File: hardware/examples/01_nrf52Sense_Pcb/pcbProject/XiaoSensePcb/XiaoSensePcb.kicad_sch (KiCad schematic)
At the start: 1 part, among them U1 Seeed Studio XIAO nRF52840

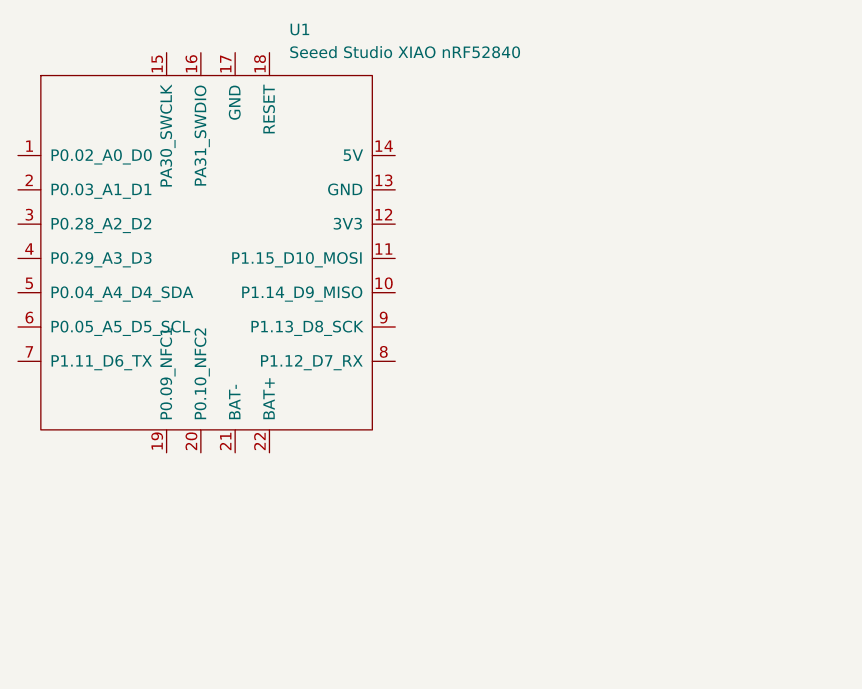
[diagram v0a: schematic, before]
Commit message: Adding kicad files for xiao sense pcb board
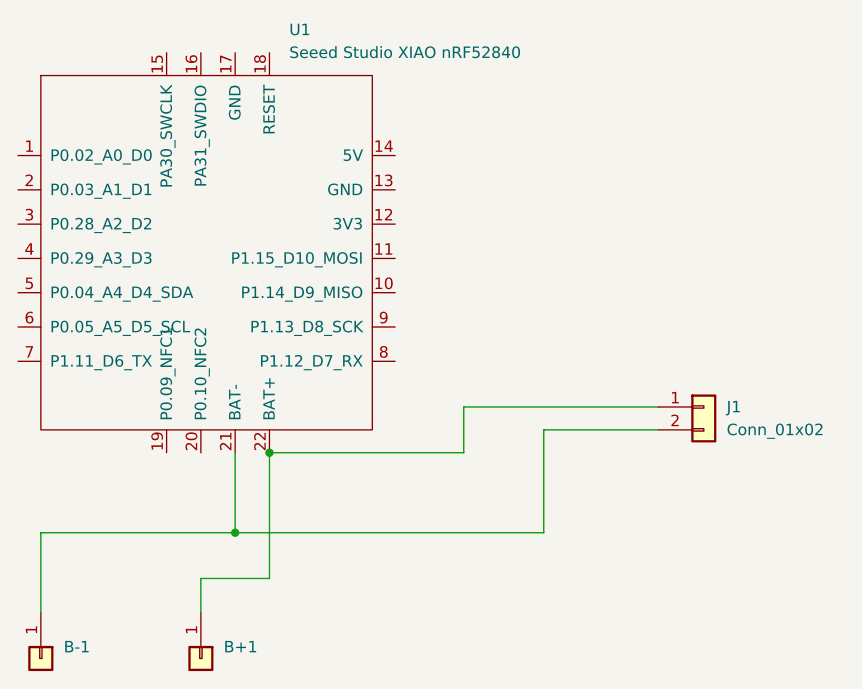
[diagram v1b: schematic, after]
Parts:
- added B+1, B-1: ~, Connector_Wire:SolderWirePad_1x01_SMD_1x2mm, symbol Connector_Generic:Conn_01x01
- added J1: Conn_01x02, Connector_JST:JST_PH_S2B-PH-SM4-TB_1x02-1MP_P2.00mm_Horizontal, symbol Connector_Generic:Conn_01x02
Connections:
- net at U1.21 (BAT-): now also B-1.1 (Pin_1), J1.2 (Pin_2)
- net at U1.22 (BAT+): now also B+1.1 (Pin_1), J1.1 (Pin_1)
